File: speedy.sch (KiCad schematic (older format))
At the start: 26 parts

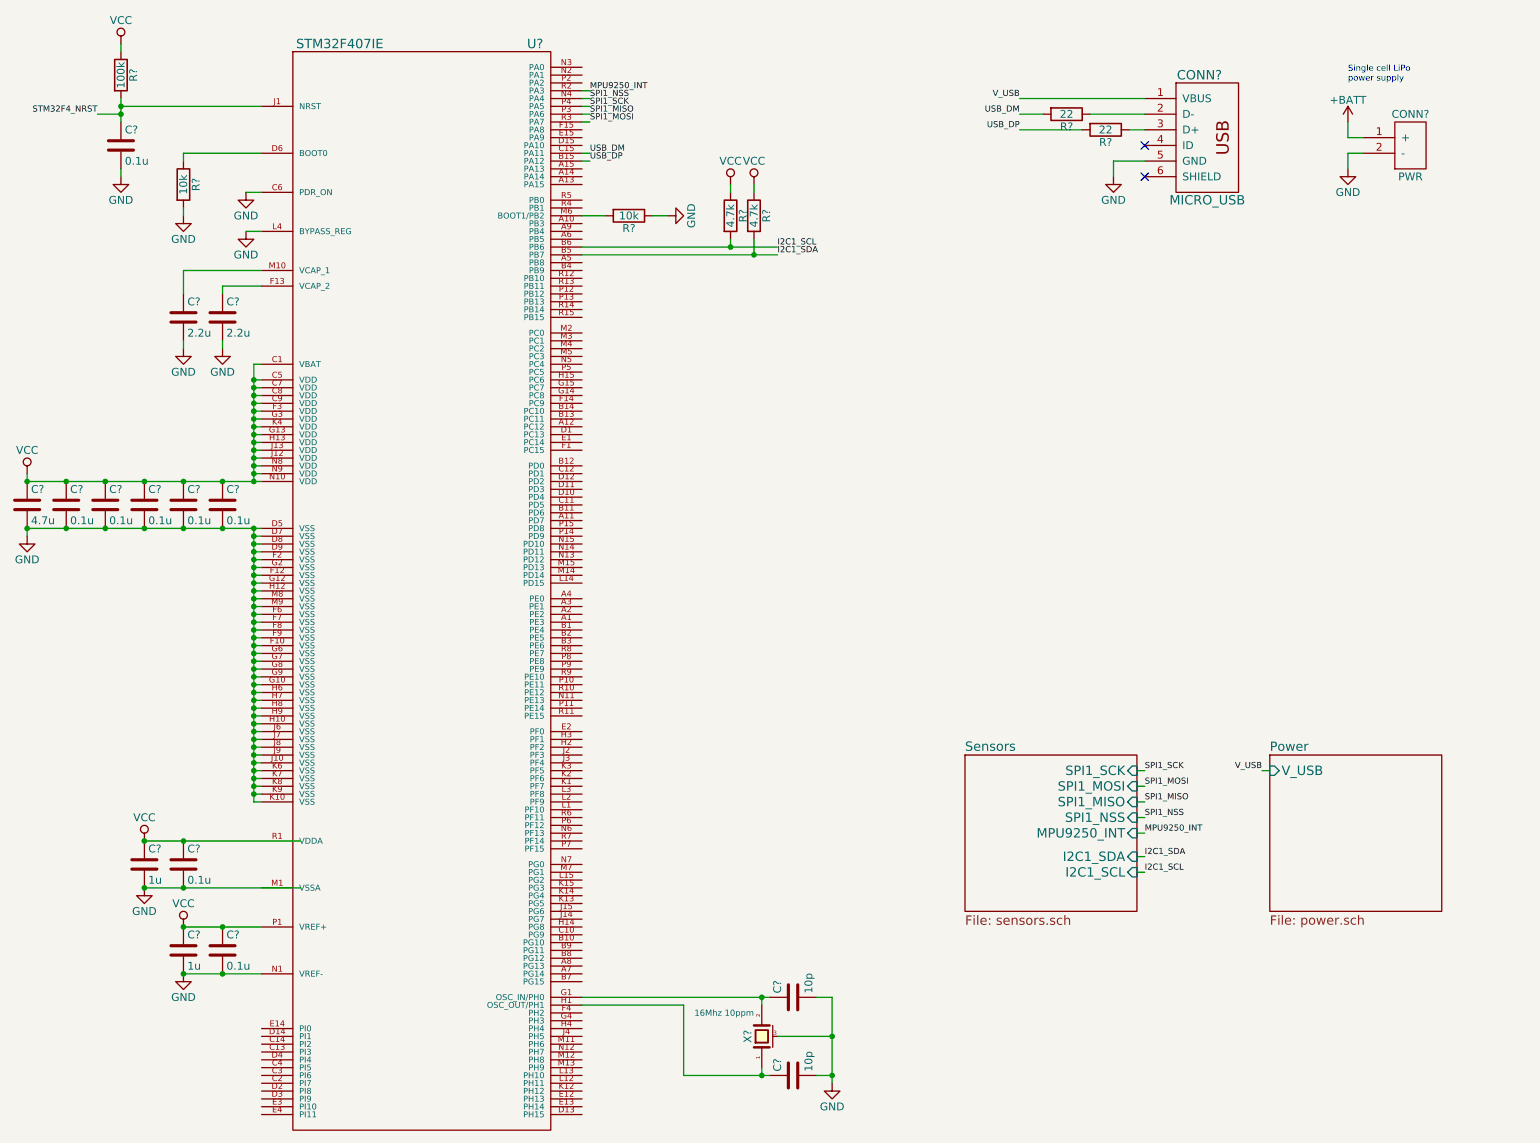
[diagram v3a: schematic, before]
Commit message: uSD card added to schematics
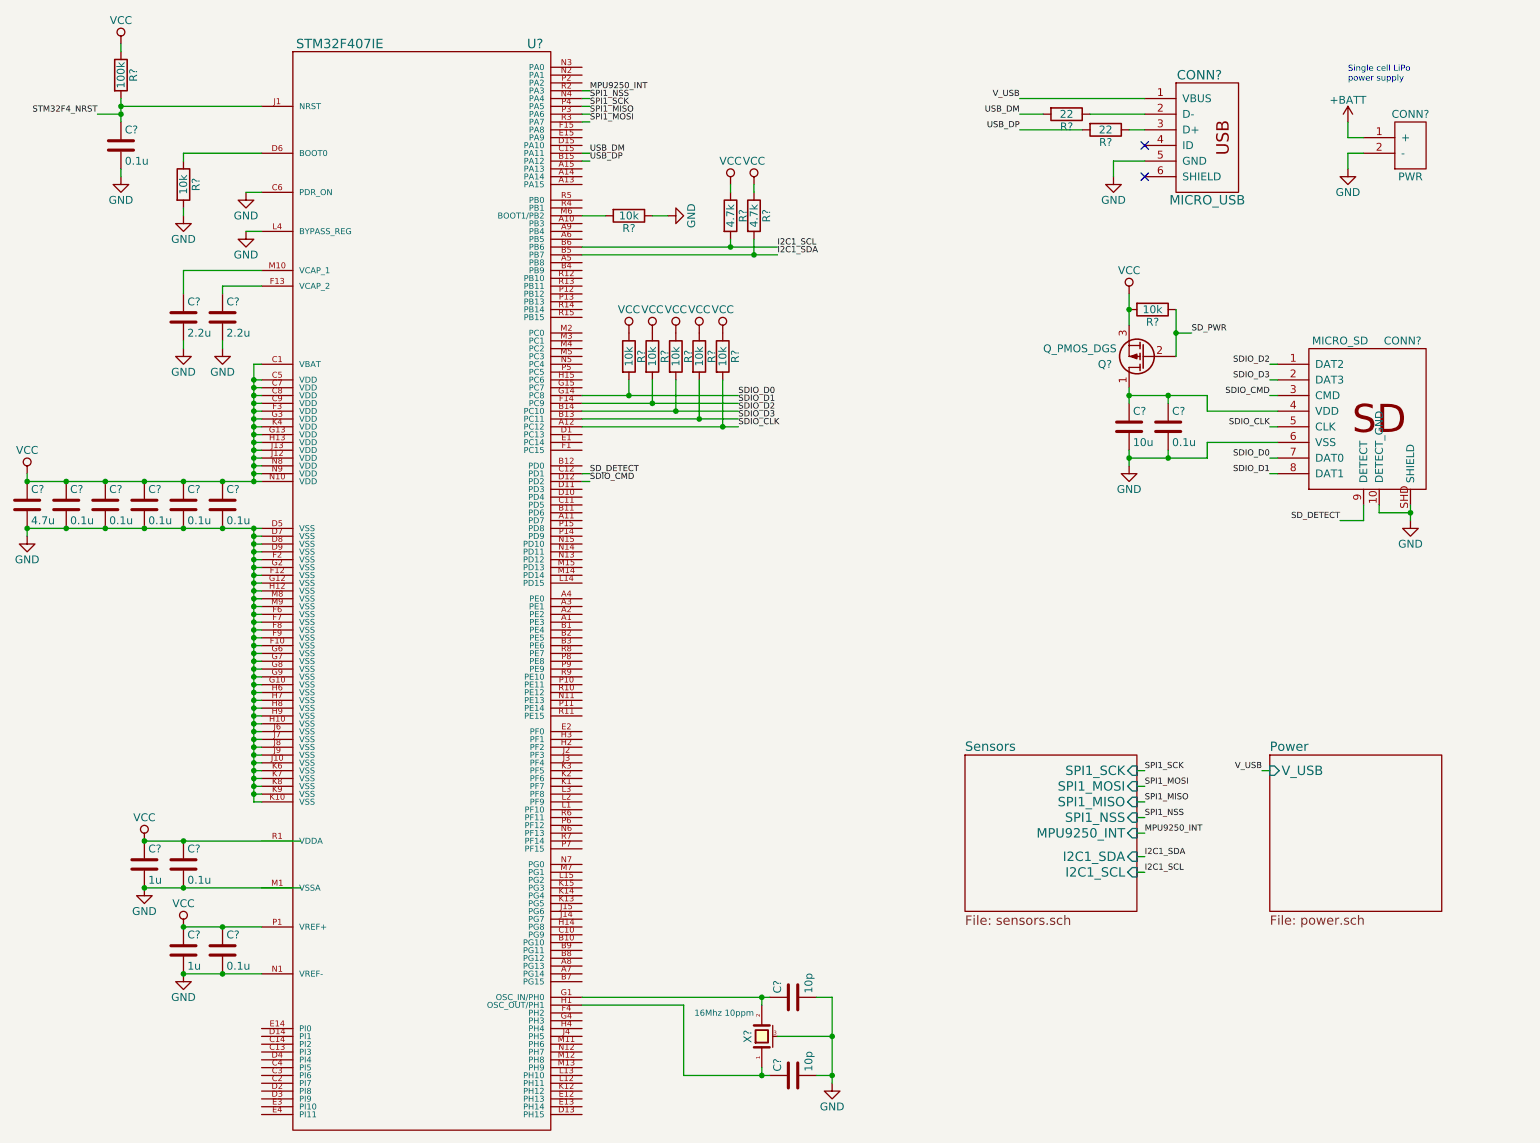
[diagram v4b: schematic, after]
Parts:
- added C?: 10u, symbol C
- added C?: 0.1u, symbol C
- added CONN?: MICRO_SD, MODULE, symbol MICRO_SD
- added Q?: Q_PMOS_DGS, symbol Q_PMOS_DGS
- added R? (x6): 10k, symbol R
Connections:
- net GND: now also C?.2, C?.2, CONN?.10 (DETECT_GND), CONN?.6 (VSS), CONN?.SHD (SHIELD)
- net VCC: now also Q?.3 (S), R?.1, R?.1, R?.1, R?.1, R?.1, R?.2
- net SDIO_CLK: now reaches U?.A12 (PC12)
- net SDIO_CLK: now also CONN?.5 (CLK), R?.2
- net SDIO_D3: now reaches U?.B13 (PC11)
- net SDIO_D3: now also CONN?.2 (DAT3), R?.2
- net SDIO_D2: now reaches U?.B14 (PC10)
- net SDIO_D2: now also CONN?.1 (DAT2), R?.2
- net SD_DETECT: now reaches U?.C12 (PD1)
- net SD_DETECT: now also CONN?.9 (DETECT)
- net SDIO_CMD: now reaches U?.D12 (PD2)
- net SDIO_CMD: now also CONN?.3 (CMD)
- net SDIO_D1: now reaches U?.F14 (PC9)
- net SDIO_D1: now also CONN?.8 (DAT1), R?.2
- net SDIO_D0: now reaches U?.G14 (PC8)
- net SDIO_D0: now also CONN?.7 (DAT0), R?.2
- new net: C?.1, C?.1, CONN?.4 (VDD), Q?.1 (D)
- new net SD_PWR: Q?.2 (G), R?.1

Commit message: CAN transceiver added in schematics
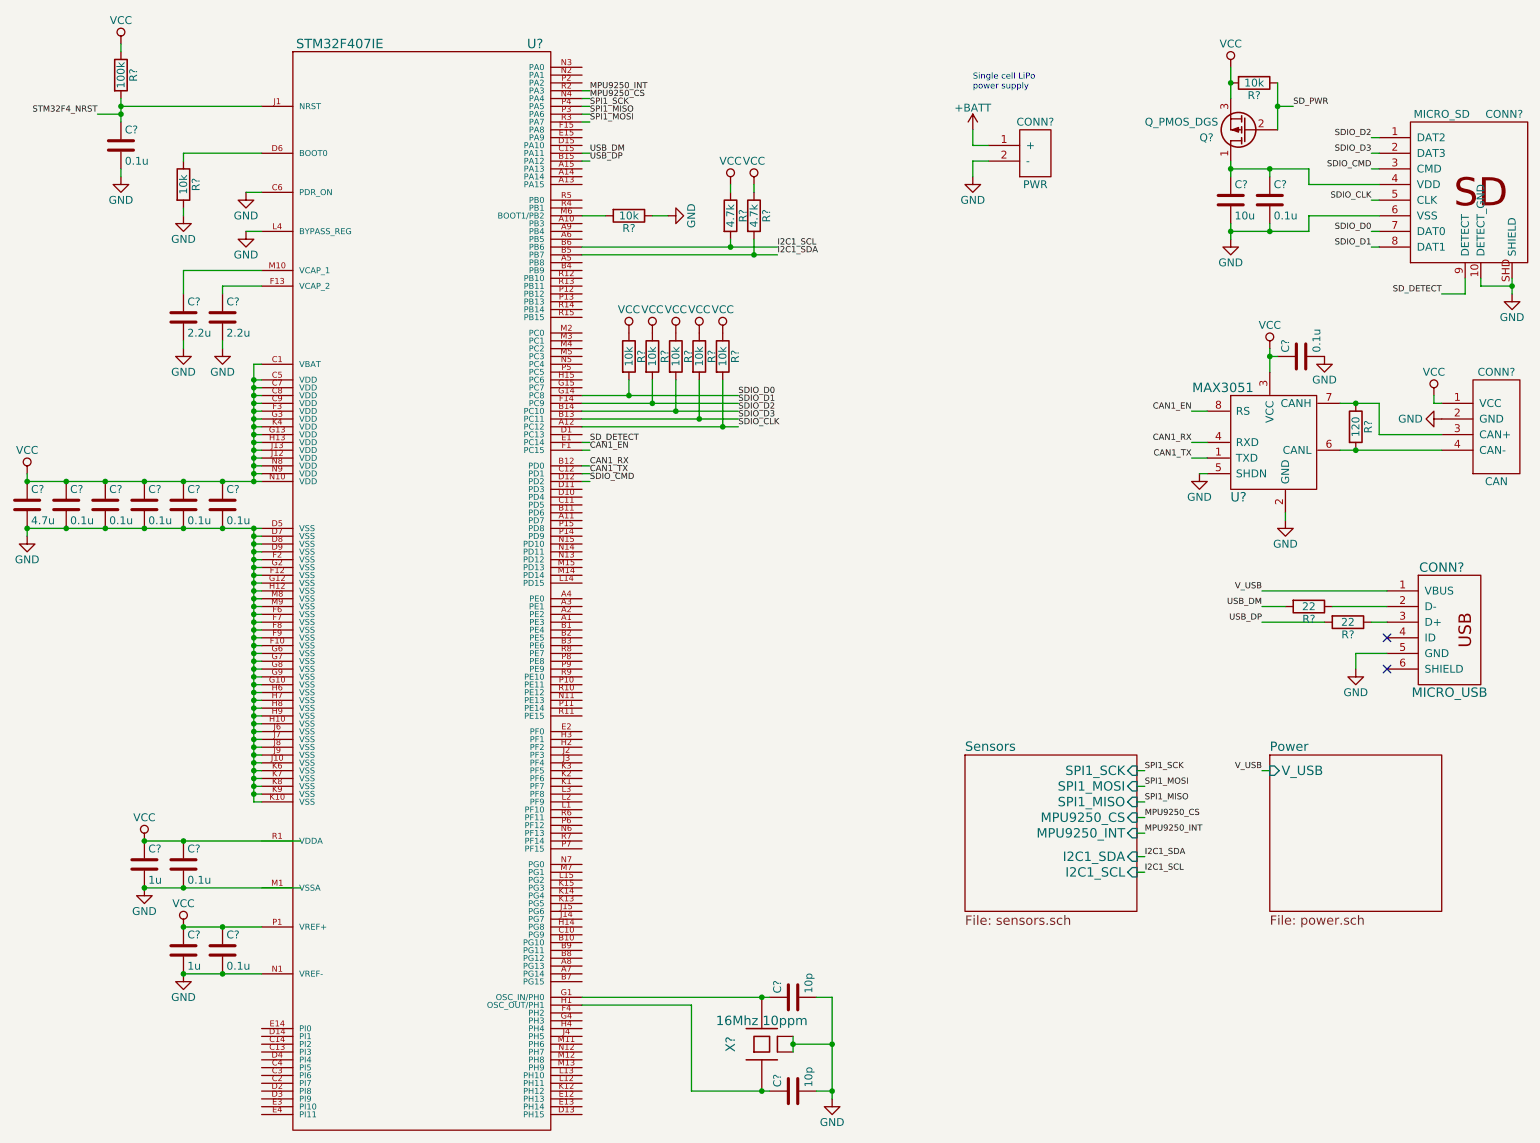
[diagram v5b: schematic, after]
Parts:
- removed X?: 16Mhz 10ppm, symbol CRYSTAL_SMD
- added C?: 0.1u, symbol C
- added CONN?: CAN, MODULE, symbol CAN
- added R?: 120, symbol R
- added U?: MAX3051, symbol MAX3051
- added X?: 16Mhz 10ppm, symbol XTAL-SMD-4-PADS
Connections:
- net GND: now also C?.2, CONN?.2 (GND), CONN?.MECH (GND), U?.2 (GND), U?.5 (SHDN), X?.2 (case), X?.4 (case)
- net SD_DETECT: now also U?.E1 (PC14); no longer U?.C12 (PD1)
- net VCC: now also C?.1, CONN?.1 (VCC), U?.3 (VCC)
- net CAN1_RX: now reaches U?.B12 (PD0)
- net CAN1_RX: now also U?.4 (RXD)
- net CAN1_EN: now reaches U?.F1 (PC15)
- net CAN1_EN: now also U?.8 (RS)
- net at C?.1, U?.G1 (OSC_IN/PH0): now also X?.3
- net at C?.1, U?.H1 (OSC_OUT/PH1): now also X?.1
- net SPI1_NSS renamed MPU9250_CS
- new net: CONN?.3 (CAN+), R?.1, U?.7 (CANH)
- new net: CONN?.4 (CAN-), R?.2, U?.6 (CANL)
- new net CAN1_TX: U?.1 (TXD), U?.C12 (PD1)
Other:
- moved on the sheet: C?, CONN?, Q?, R?

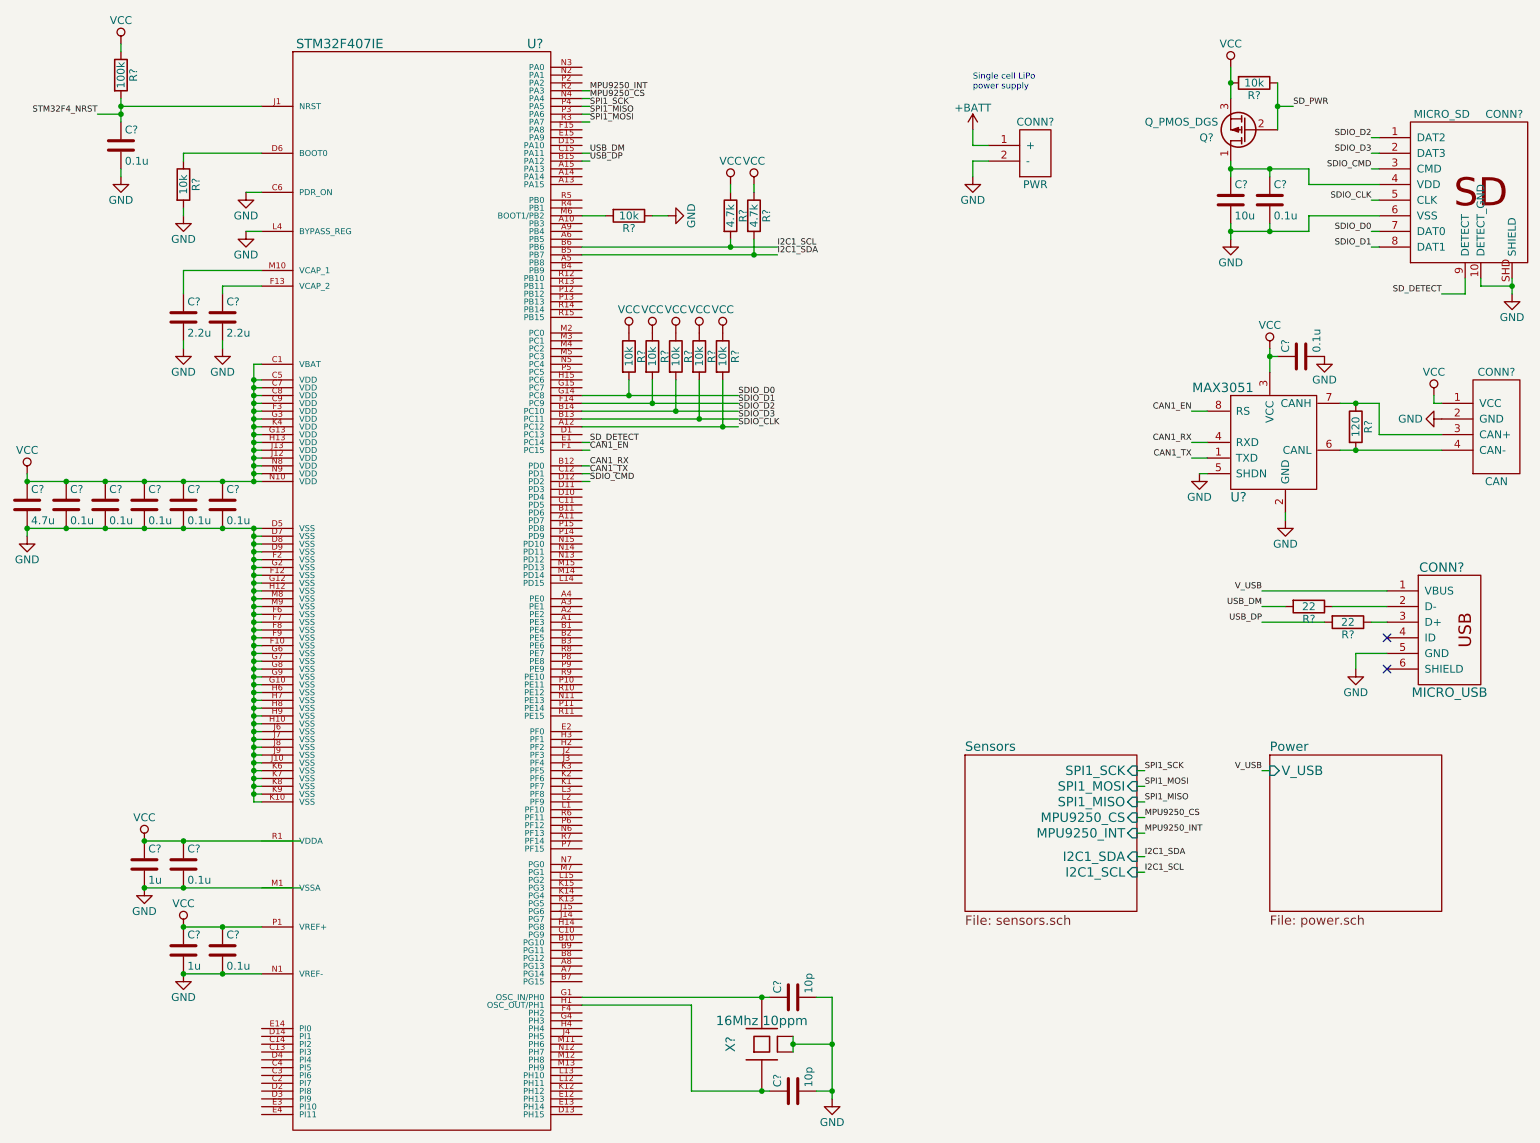
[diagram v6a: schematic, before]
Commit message: Second CAN connector for daisy chain
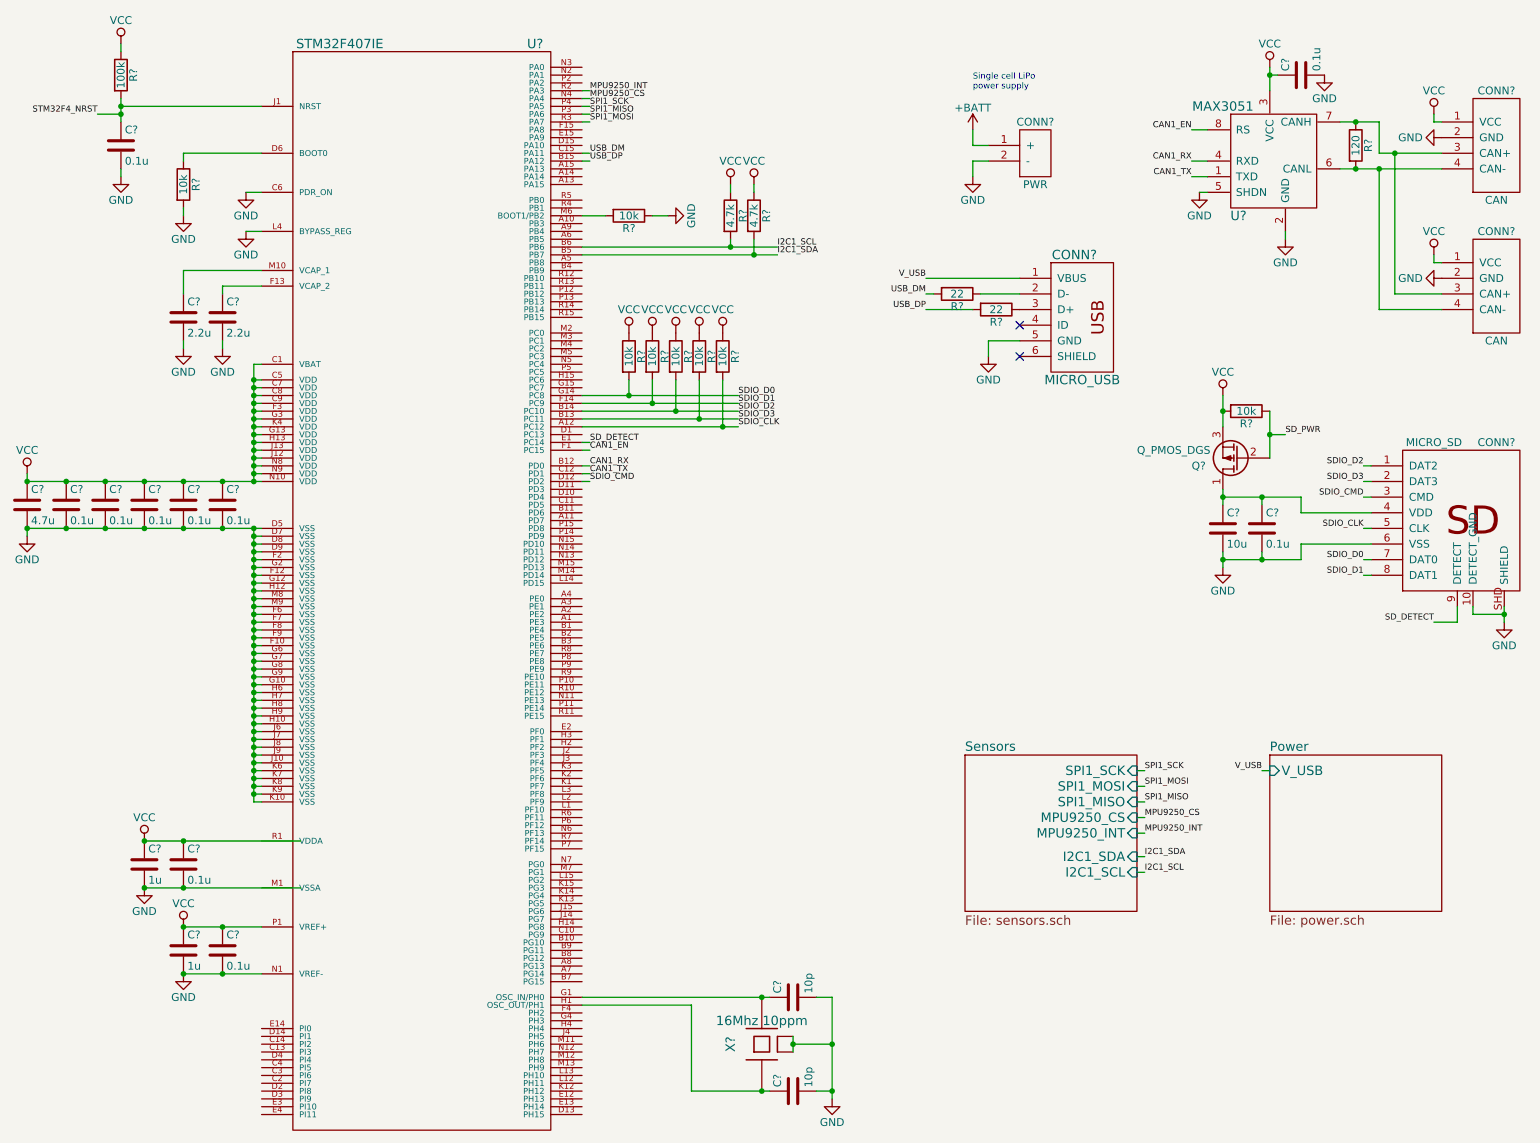
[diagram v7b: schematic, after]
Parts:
- added CONN?: CAN, MODULE, symbol CAN
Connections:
- net GND: now also CONN?.2 (GND), CONN?.MECH (GND)
- net VCC: now also CONN?.1 (VCC)
- net at CONN?.3 (CAN+), R?.1, U?.7 (CANH): now also CONN?.3 (CAN+)
- net at CONN?.4 (CAN-), R?.2, U?.6 (CANL): now also CONN?.4 (CAN-)
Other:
- moved on the sheet: C?, CONN?, Q?, R?, U?
